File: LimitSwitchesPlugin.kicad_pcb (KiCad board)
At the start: 2 copper layers, 8 parts, among them J0 CONN_02X16

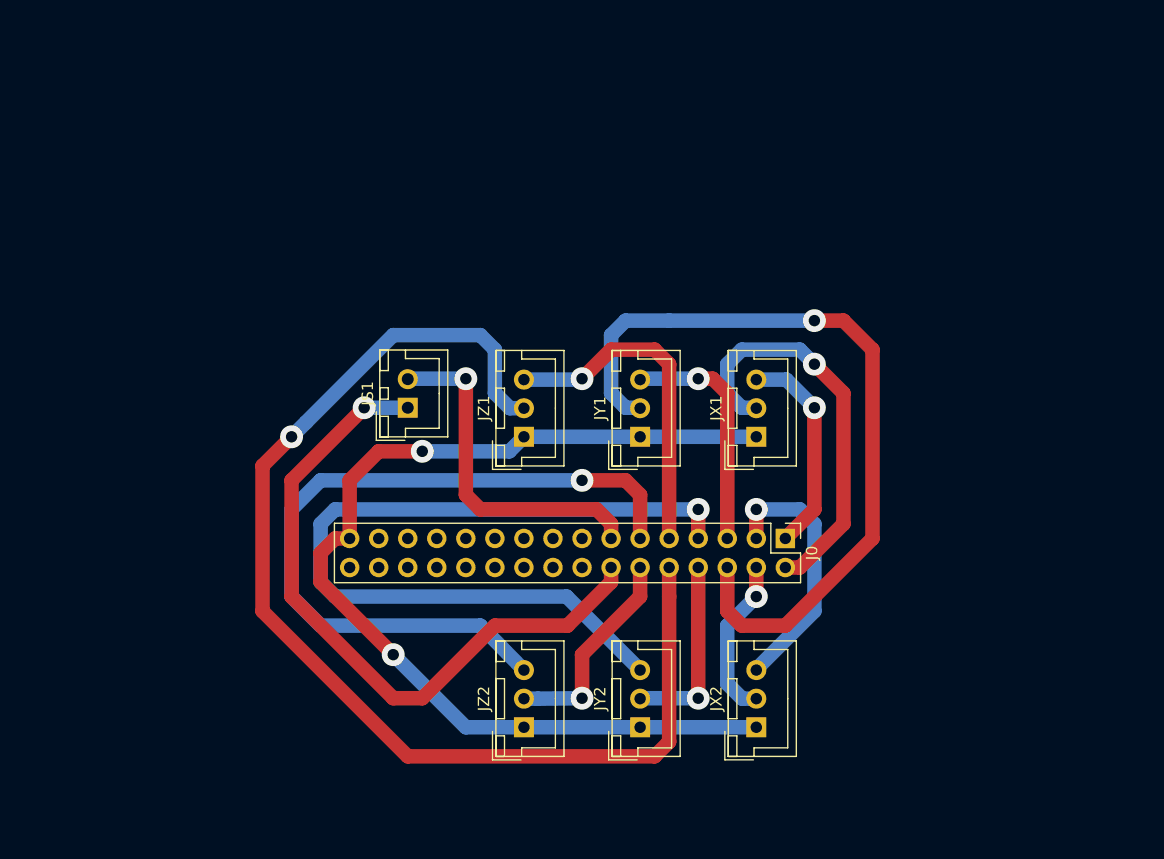
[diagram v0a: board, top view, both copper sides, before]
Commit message: One row layout
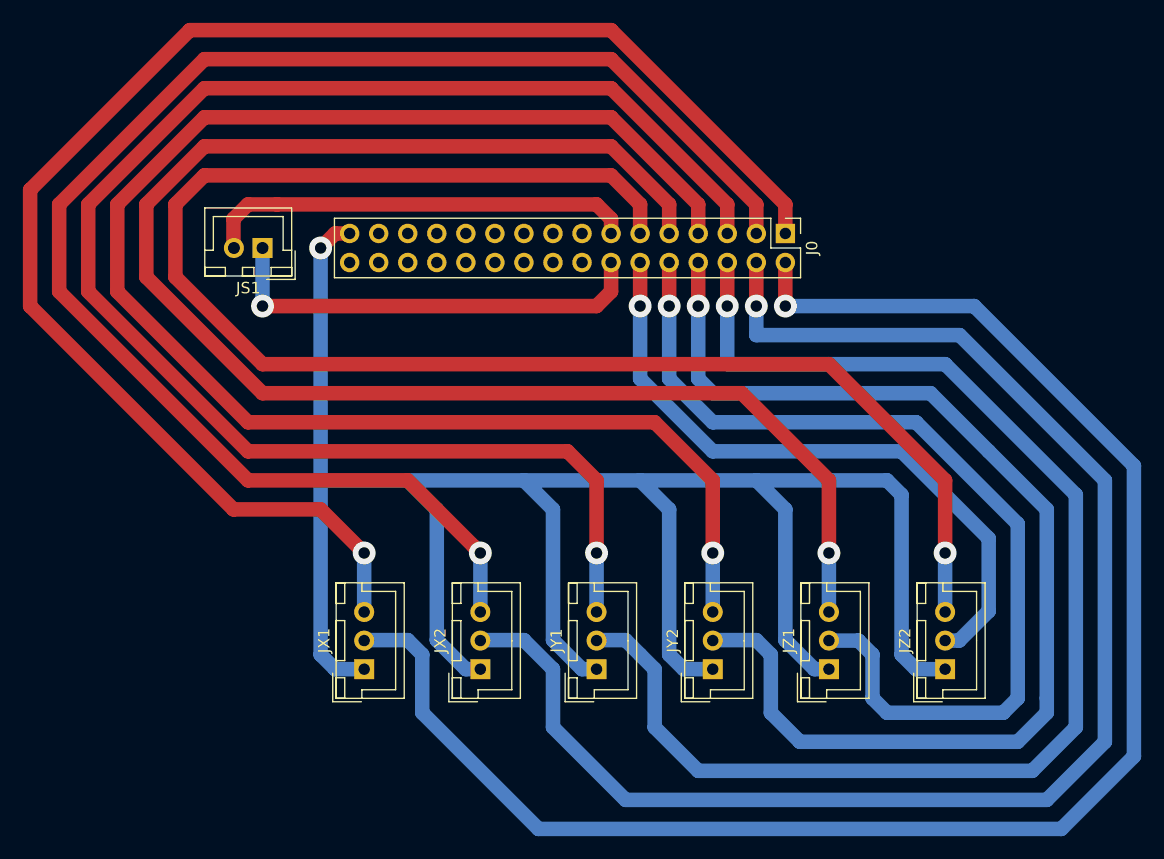
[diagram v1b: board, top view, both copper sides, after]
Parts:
- moved JX1 39.9 mm to (142.2, 102.9)
- moved JZ2 37.2 mm to (193.0, 102.9)
- moved JZ1 33.5 mm to (182.9, 102.9)
- moved J0 26.7 mm to (179.1, 64.8)
- moved JX2 24.7 mm to (152.4, 102.9)
- moved JY1 20.7 mm to (162.6, 102.9)
- moved JS1 18.9 mm to (133.3, 66.0), turned to 180 degrees
- moved JY2 8.13 mm to (172.7, 102.9)
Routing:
- net Net-(J0-Pad5): track 20.9 -> 137.3 mm
- net Net-(J0-Pad4): track 14.3 -> 130.4 mm
- net Net-(J0-Pad1): track 18.6 -> 134.2 mm
- net Net-(J0-Pad3): track 23.0 -> 133.1 mm
- net Net-(J0-Pad2): track 36.0 -> 145.2 mm
- net Net-(J0-Pad9): track 29.6 -> 137.4 mm
- net Net-(J0-Pad31): track 91.2 -> 192.9 mm, vias 2 -> 1
- net Net-(J0-Pad8): track 16.5 -> 100.1 mm
- net Net-(J0-Pad11): track 66.5 -> 137.8 mm
- net Net-(J0-Pad7): track 72.3 -> 137.7 mm
- net Net-(J0-Pad6): track 69.3 -> 115.6 mm
- net Net-(J0-Pad12): track 18.6 -> 57.7 mm
- net Net-(J0-Pad14): track 60.1 -> 38.6 mm
- net Net-(J0-Pad10): track 101.8 -> 83.0 mm
- net Net-(J0-Pad13): track 30.3 -> 37.9 mm, vias 1 -> 0

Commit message: More compact resolution
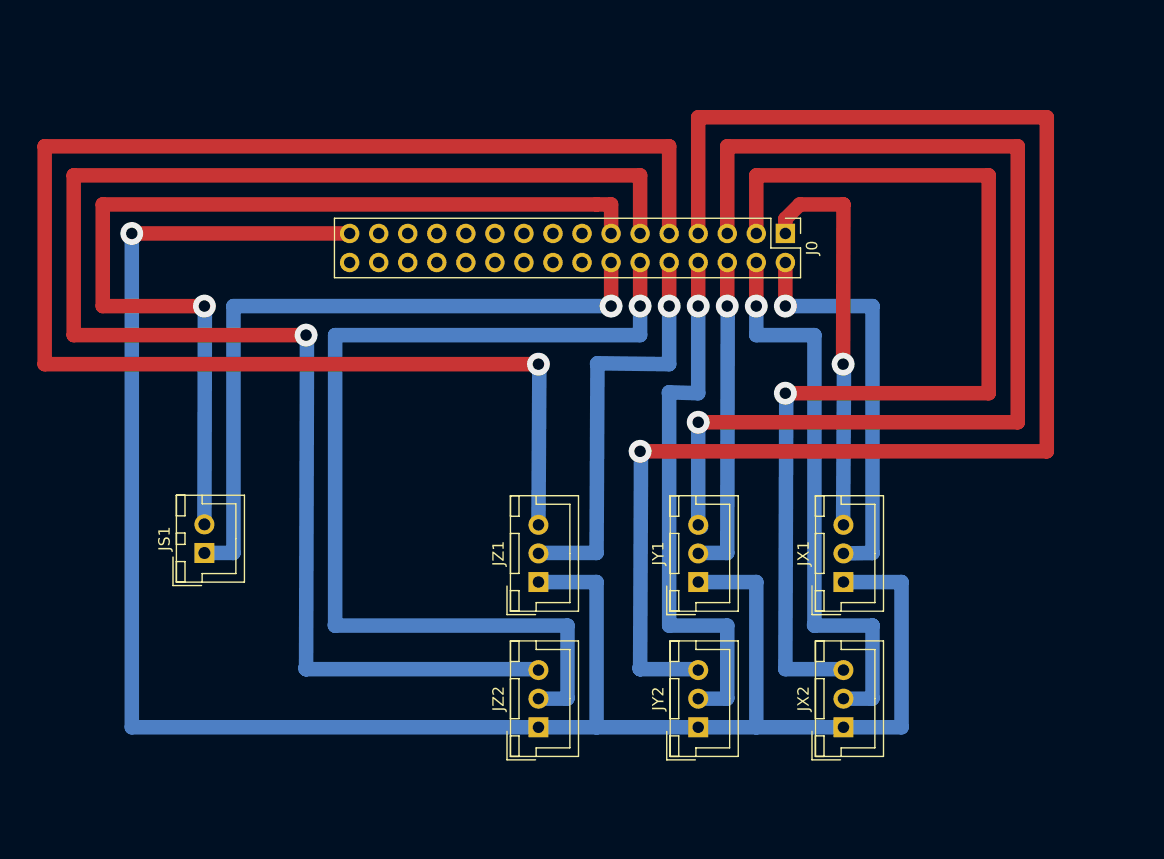
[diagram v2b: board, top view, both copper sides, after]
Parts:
- moved JX1 42.6 mm to (184.2, 95.2)
- moved JZ2 35.9 mm to (157.5, 108.0)
- moved JX2 32.2 mm to (184.2, 108.0)
- moved JS1 27.1 mm to (128.3, 92.7), turned to 90 degrees
- moved JZ1 26.5 mm to (157.5, 95.2)
- moved JY1 11.7 mm to (171.4, 95.2)
- moved JY2 5.24 mm to (171.4, 108.0)
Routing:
- net Net-(J0-Pad2): track 145.2 -> 35.7 mm
- net Net-(J0-Pad1): track 134.2 -> 35.2 mm
- net Net-(J0-Pad6): track 115.6 -> 28.0 mm
- net Net-(J0-Pad4): track 130.4 -> 50.9 mm
- net Net-(J0-Pad8): track 100.1 -> 48.4 mm
- net Net-(J0-Pad10): track 83.0 -> 36.9 mm
- net Net-(J0-Pad13): track 37.9 -> 83.9 mm, vias 0 -> 1
- net Net-(J0-Pad5): track 137.3 -> 94.5 mm
- net Net-(J0-Pad3): track 133.1 -> 91.6 mm
- net Net-(J0-Pad12): track 57.7 -> 87.7 mm
- net Net-(J0-Pad14): track 38.6 -> 61.0 mm
- net Net-(J0-Pad31): track 192.9 -> 182.9 mm
- net Net-(J0-Pad7): track 137.7 -> 129.7 mm
- net Net-(J0-Pad9): track 137.4 -> 138.6 mm
- net Net-(J0-Pad11): track 137.8 -> 138.6 mm

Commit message: Redesign of the board with all connectors beneath the pin headers
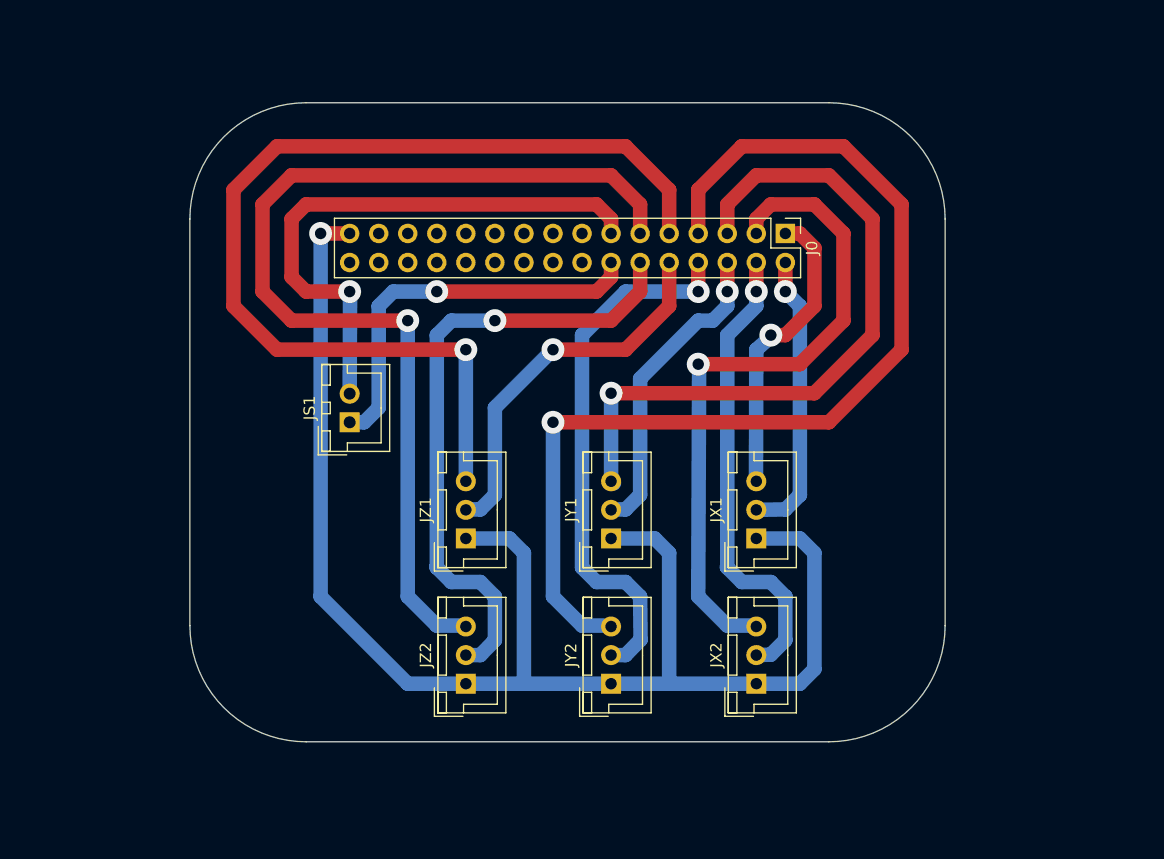
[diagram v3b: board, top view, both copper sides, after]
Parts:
- moved JS1 17.1 mm to (141.0, 81.3)
- moved JX1 8.52 mm to (176.5, 91.4)
- moved JX2 8.52 mm to (176.5, 104.1)
- moved JY1 8.52 mm to (163.8, 91.4)
- moved JY2 8.52 mm to (163.8, 104.1)
- moved JZ1 7.41 mm to (151.1, 91.4)
- moved JZ2 7.41 mm to (151.1, 104.1)
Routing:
- net Net-(J0-Pad31): track 182.9 -> 131.0 mm
- net Net-(J0-Pad9): track 138.6 -> 88.9 mm
- net Net-(J0-Pad11): track 138.6 -> 89.4 mm
- net Net-(J0-Pad7): track 129.7 -> 92.6 mm
- net Net-(J0-Pad13): track 83.9 -> 49.9 mm
- net Net-(J0-Pad5): track 94.5 -> 61.1 mm
- net Net-(J0-Pad3): track 91.6 -> 59.0 mm
- net Net-(J0-Pad12): track 87.7 -> 55.3 mm
- net Net-(J0-Pad14): track 61.0 -> 34.6 mm
- net Net-(J0-Pad2): track 35.7 -> 25.3 mm
- net Net-(J0-Pad4): track 50.9 -> 40.8 mm
- net Net-(J0-Pad1): track 35.2 -> 26.7 mm
- net Net-(J0-Pad10): track 36.9 -> 33.4 mm
- net Net-(J0-Pad8): track 48.4 -> 47.7 mm
- net Net-(J0-Pad6): track 28.0 -> 28.6 mm
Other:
- board outline added: 66 x 55.9 mm
